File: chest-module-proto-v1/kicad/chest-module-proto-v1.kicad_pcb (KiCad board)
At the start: 2 copper layers, 110 x 90 mm, 96 parts, among them J1 USB_C_Receptacle_USB2.0, J2 Conn_01x06_Male, J3 Conn_01x06_Male, J4 SWD, Q1 SS8050-G, Q2 SS8050-G, U1 AMS1117-3.3, U10 74HC00, U11 IRM-H6XXT, U12 IRM-H6XXT, U13 STM32G030Fx, U2 TP4056, U3 TPS61230ARNSR, U4 DW01, U5 FS8205A, U6 74HC00, U7 ESP32-WROOM-32, U8 USBLC6-2SC6, U9 CP2102N-Axx-xQFN28

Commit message: Renamed strings
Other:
- board text added: "Skirmish Chest Module (Proto V1) Design / (C) 2023 Ole Lange"
- board text removed: "Skirmish Breast Module (Proto V1) Design / (C) 2023 Ole Lange"
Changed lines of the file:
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@@
   (paper "A4")
   (title_block
-    (title "Skirmish Breast Module")
+    (title "Skirmish Chest Module")
     (date "2023-01-29")
     (rev "Proto V1")
@@
     (effects (font (size 1.5 1.5) (thickness 0.25)))
   )
-  (gr_text "Skirmish Breast Module (Proto V1)\nDesign / (C) 2023 Ole Lange" (at 145.5 80.75) (layer "F.SilkS")
+  (gr_text "Skirmish Chest Module (Proto V1)\nDesign / (C) 2023 Ole Lange" (at 145.5 80.75) (layer "F.SilkS")
     (effects (font (size 2 2) (thickness 0.4)))
   )

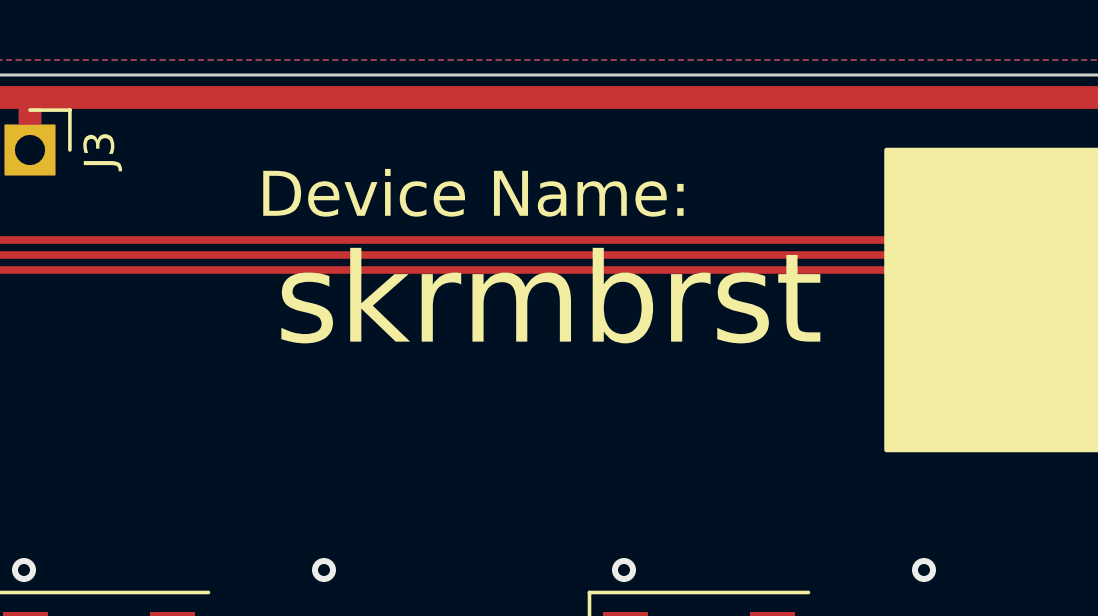
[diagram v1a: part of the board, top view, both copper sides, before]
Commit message: skrmbrst to skrmvest
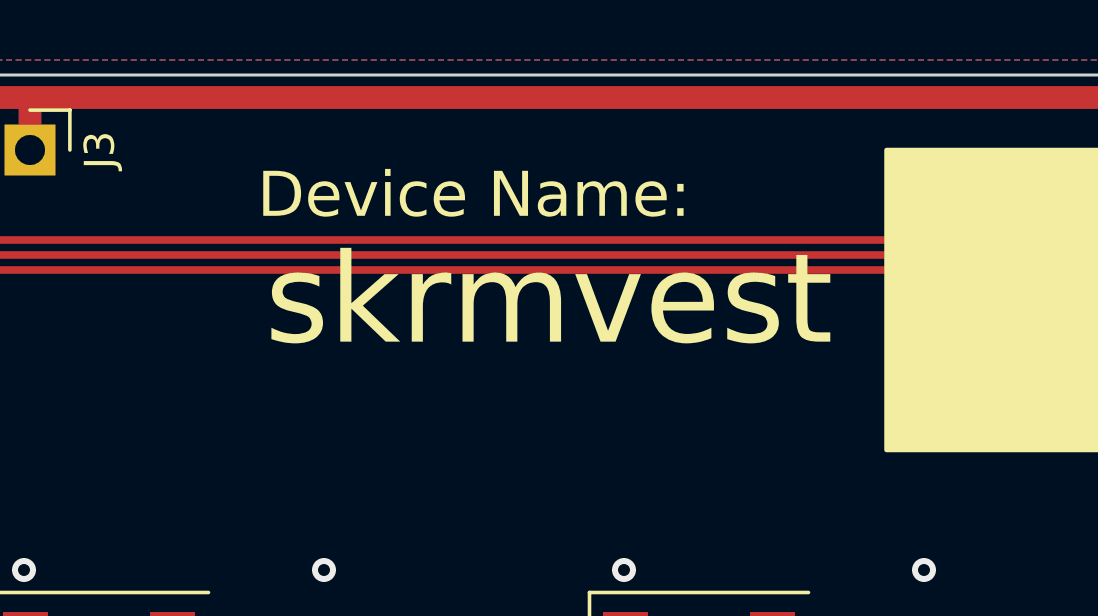
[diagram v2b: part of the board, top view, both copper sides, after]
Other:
- board text added: "skrmvest"
- board text removed: "skrmbrst"
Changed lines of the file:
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@@
     (effects (font (size 2 2) (thickness 0.4)))
   )
-  (gr_text "skrmbrst" (at 130.5 59) (layer "F.SilkS")
+  (gr_text "skrmvest" (at 130.5 59) (layer "F.SilkS")
     (effects (font (size 3 3) (thickness 0.5)))
   )
